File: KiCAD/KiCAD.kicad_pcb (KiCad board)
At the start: 2 copper layers, 200 x 150 mm, 174 parts, among them J1 Conn_01x02_Pin, J10 Paddle, J11 GRID_BIAS, J12 CATHODE_SENSE, J13 Conn_01x05, J14 Conn_01x02_Pin, J15 Conn_01x03_Pin, J2 Conn_01x02_Pin, J3 Conn_01x02_Pin, J4 8P8C_Shielded, J5 ENC_INT if needed, J6 TX/RX, J7 HV, J8 HV_INRUSH_BYPASS, J9 TR_SENSE, Q1 J310, Q2 2N7000, Q3 2N7000, Q4 2N7000, Q5 2N7000, Q6 2N7000, Q7 2N7000, T1 2N3906, T2 2N3906, U1 Si5351A_Breakout, U10 OPA454, U11 LM4040LP-5, U12 LM393, U13 OPA1641, U14 OPA1641, U16 AM26LS32ACN, U17 Adafruit_PCF8575_Breakout, U18 CD14538B, U3 MC1496, U4 MCP4921, U5 OPA454, U6 LM7171xIN, U7 LM7171xIN, U8 MCP4728, U9 LM7805_TO220

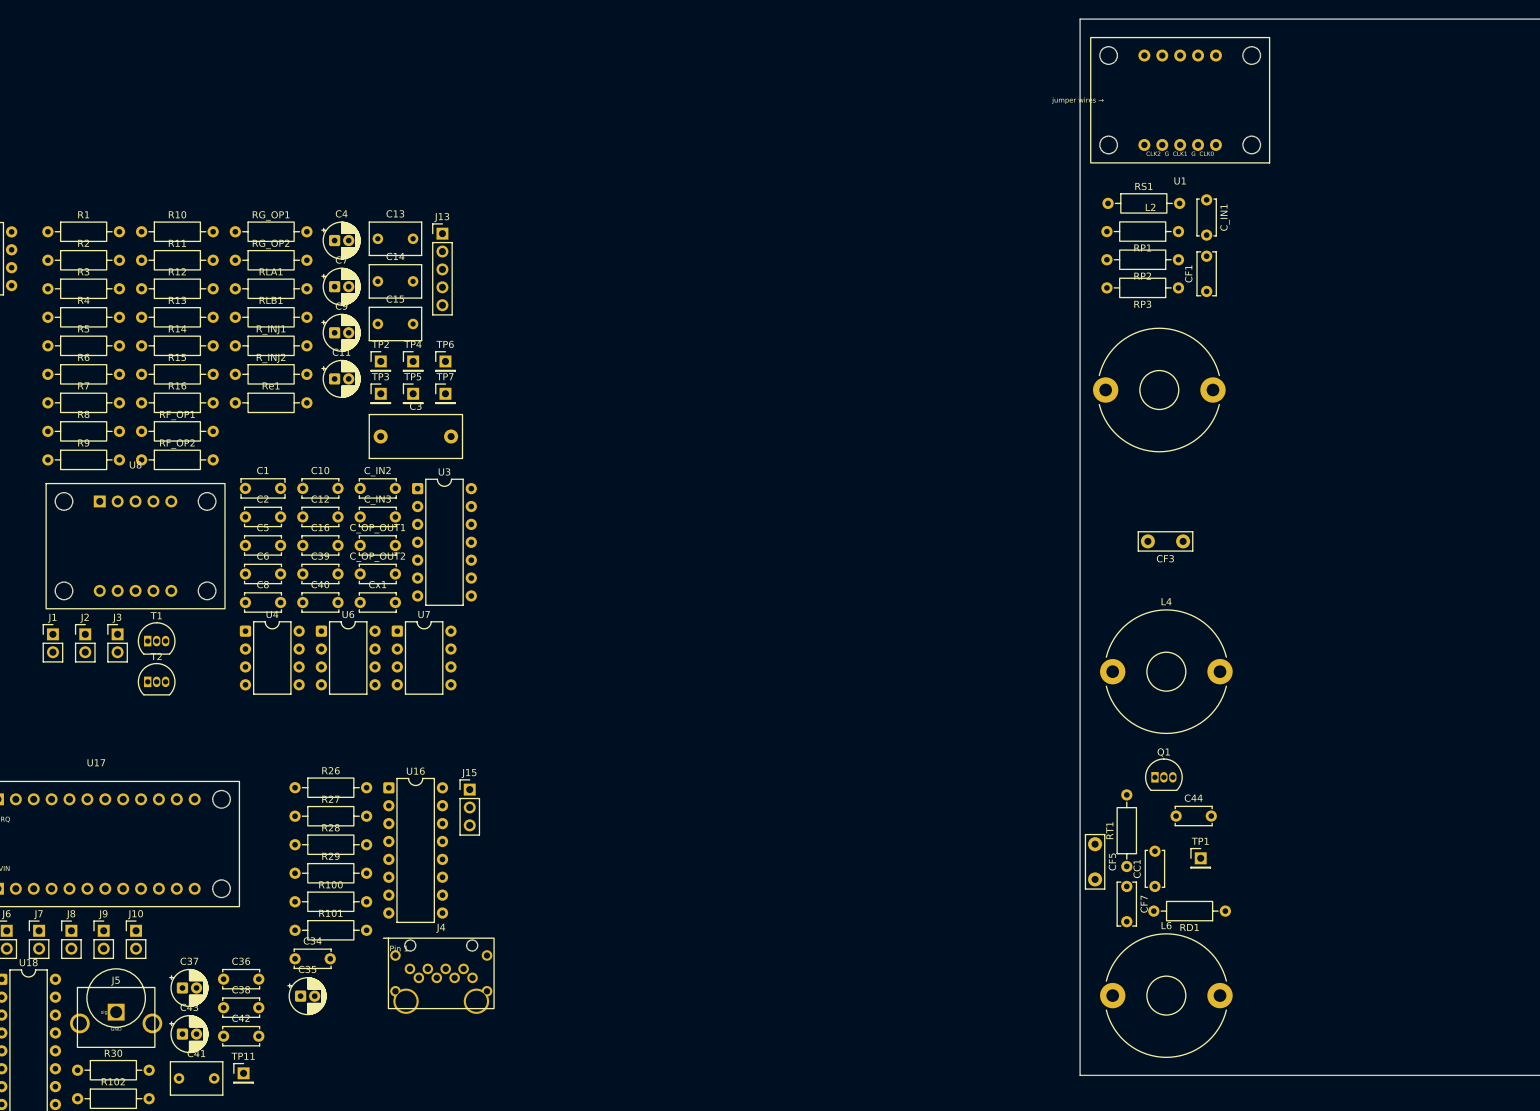
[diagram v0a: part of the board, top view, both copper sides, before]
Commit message: kicad: buffer_keyer partial placement + MCP4728 footprint rebuild
- KiCAD.kicad_pcb: initial placement of 19 buffer_keyer parts (MC1496
  keyer, T1/T2 2N3906s, VEE divider R7/R8, LM4040, C4 10uF bulk, R_INJ1
  and adjacent passives) on the 200x150 board alongside the completed
  VFO block. Zero routing yet.
- Adafruit_MCP4728_Breakout.kicad_mod: rebuild for the correct 2 x 6-pin
  physical layout (was 5+5). Top row JP2 = GND VA VB VC VD VCC, bottom
  row JP1 = VCC GND SCL SDA LDAC RDY. Duplicate VCC/GND pads share
  pad numbers (1,2) so they tie to the same nets as the symbol's VIN/GND.
  Silk labels rebuilt as 12 per-pin fp_text items centered on each pin's
  X coordinate for clear placement verification.
- buffer_keyer.kicad_sch: two 100nF VEE-to-GND decoupling caps added at
  T1 and T2.

Co-Authored-By: Claude Opus 4.7 <noreply@anthropic.com>
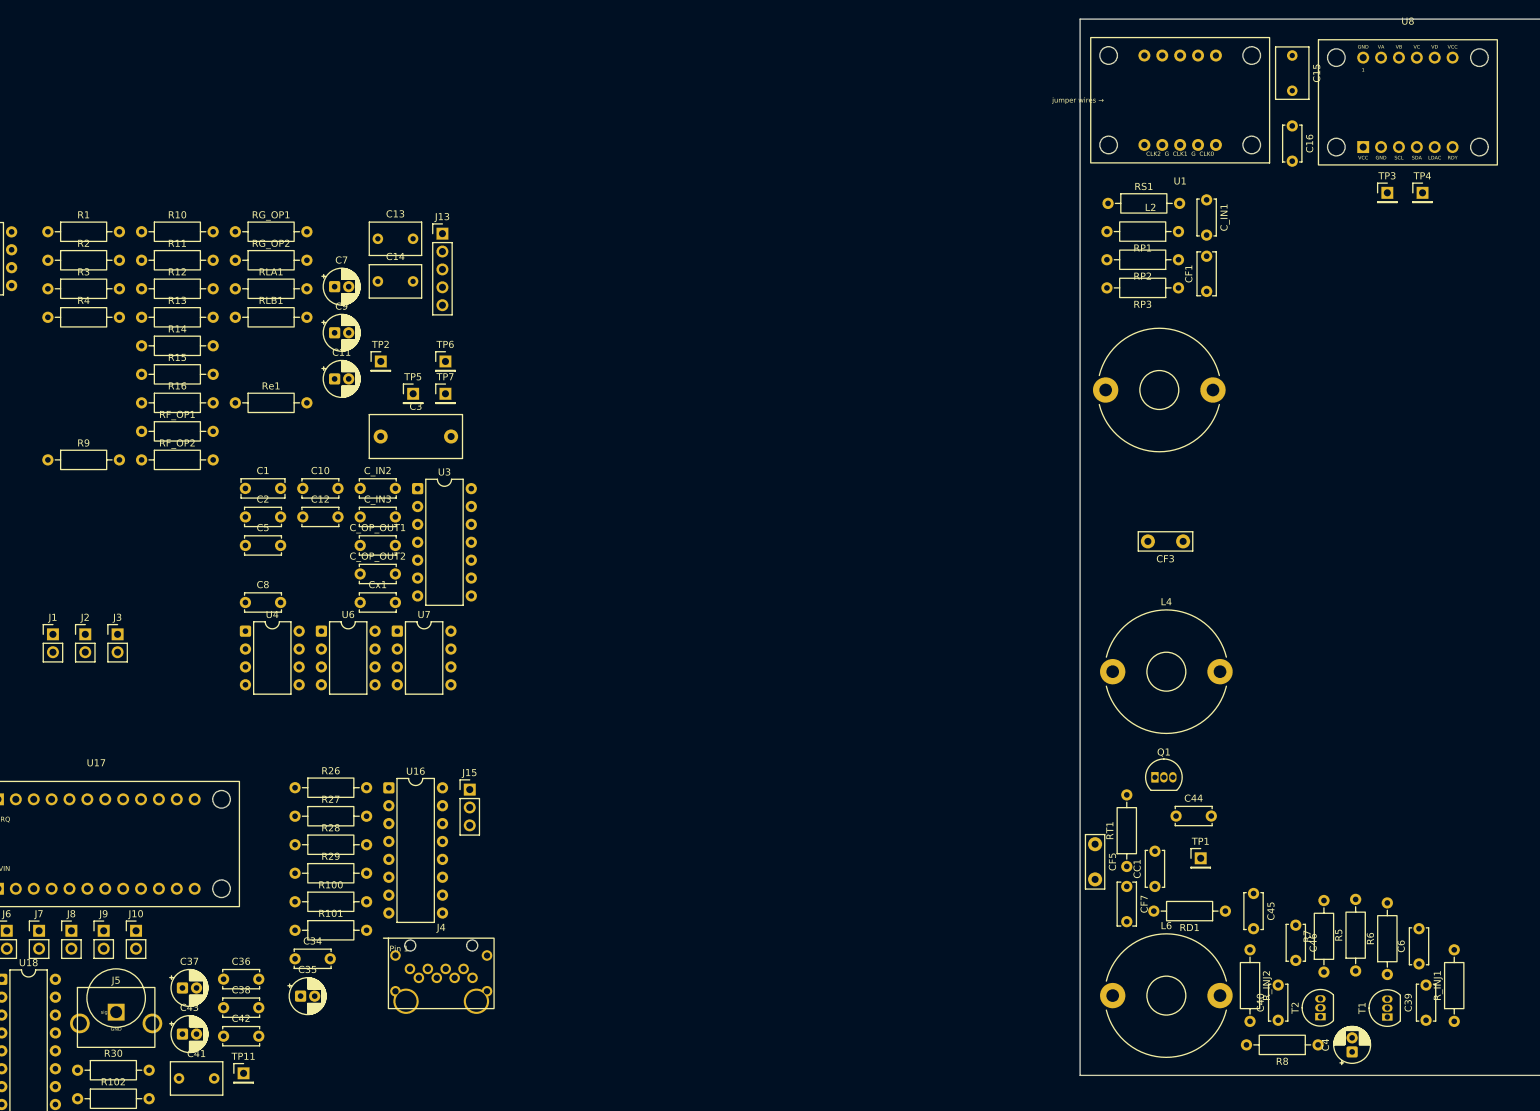
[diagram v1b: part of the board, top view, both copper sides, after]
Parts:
- added C45: 100nF, Capacitor_THT:C_Disc_D5.0mm_W2.5mm_P5.00mm, F.Cu at (40.5, 138.5)
- added C46: 100nF, Capacitor_THT:C_Disc_D5.0mm_W2.5mm_P5.00mm, F.Cu at (46.5, 143.0)
- moved R6 208.4 mm to (59.5, 150.0), turned to 90 degrees
- moved R5 205.8 mm to (55.0, 149.5), turned to 90 degrees
- moved R8 200.3 mm to (49.7, 160.0), turned to 180 degrees
- moved R7 198.4 mm to (50.5, 149.7), turned to 90 degrees
- moved R_INJ1 197.9 mm to (69.0, 156.7), turned to 90 degrees
- moved U8 191.4 mm to (62.4, 26.1)
- moved C4 184.8 mm to (54.5, 161.0), turned to 90 degrees
- moved T1 184.0 mm to (59.5, 156.0), turned to 90 degrees
- moved C6 175.6 mm to (64.0, 148.5), turned to 90 degrees
- moved T2 173.2 mm to (50.0, 156.0), turned to 90 degrees
- moved C39 171.6 mm to (65.0, 156.5), turned to 90 degrees
- moved R_INJ2 165.7 mm to (40.0, 146.5), turned to -90 degrees
- moved C16 152.6 mm to (46.0, 29.5), turned to -90 degrees
- moved C40 150.7 mm to (44.0, 156.5), turned to 90 degrees
- moved TP3 145.8 mm to (59.5, 39.0)
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
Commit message: kicad: T68-6 hand-wound toroid footprints (flat + vertical)
- xmitter.pretty/T68-6_Flat_HandWound.kicad_mod: flat mount for L2/L6.
  Both leads exit on the same radial side -- outer pad at (0, -10.0)
  1.23 mm outside OD, inner pad at (0, -2.5) inside the ID hole.
  Pitch 7.5 mm. Silk shows OD (17.53 mm) + ID (9.40 mm) circles.
- xmitter.pretty/T68-6_Vertical_HandWound.kicad_mod: on-edge mount for L4.
  Top-down projection = OD x HT (17.53 x 4.83 mm) rectangle. Pads at
  (-2.0, -4.5) and (+2.0, +4.5) -- above and below the rectangle with
  the diagonal offset that matches natural lead exit after 4-turn winding.
- vfo.kicad_sch: L2/L4/L6 footprint fields switched to the new project
  footprints (was Inductor_THT:L_Toroid_Horizontal_D17.3mm_P15.24mm_Bourns_2000
  which is a pre-wound Bourns part, not a hand-wound toroid).
- Documentation/flat-toroid.jpg: reference drawing showing lead
  arrangement for both mount styles.

Nominal L per inductor with 4 turns of 22/24 AWG magnet wire evenly
spaced: A_L(T68-6) * 4^2 = 47 * 16 = 752 nH (target 736 nH, +2.2%).

Co-Authored-By: Claude Opus 4.7 <noreply@anthropic.com>
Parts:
- L2, L6: footprint Inductor_THT:L_Toroid_Horizontal_D17.3mm_P15.24mm_Bourns_2000 -> xmitter:T68-6_Flat_HandWound
- L4: footprint Inductor_THT:L_Toroid_Horizontal_D17.3mm_P15.24mm_Bourns_2000 -> xmitter:T68-6_Vertical_HandWound
- moved C1 265.1 mm to (162.4, 75.8)
- moved C10 265.1 mm to (170.6, 75.8)
- moved C11 265.1 mm to (175.1, 60.2)
- moved C12 265.1 mm to (170.6, 79.8)
- moved C13 265.1 mm to (181.2, 40.3)
- moved C14 265.1 mm to (181.2, 46.4)
- moved C2 265.1 mm to (162.4, 79.8)
- moved C5 265.1 mm to (162.4, 83.8)
- moved C7 265.1 mm to (175.1, 47.1)
- moved C8 265.1 mm to (162.4, 92.0)
- moved C9 265.1 mm to (175.1, 53.6)
- moved J13 265.1 mm to (190.4, 39.6)
- moved R1 265.1 mm to (134.4, 39.3)
- moved R10 265.1 mm to (147.7, 39.3)
- moved R11 265.1 mm to (147.7, 43.4)
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
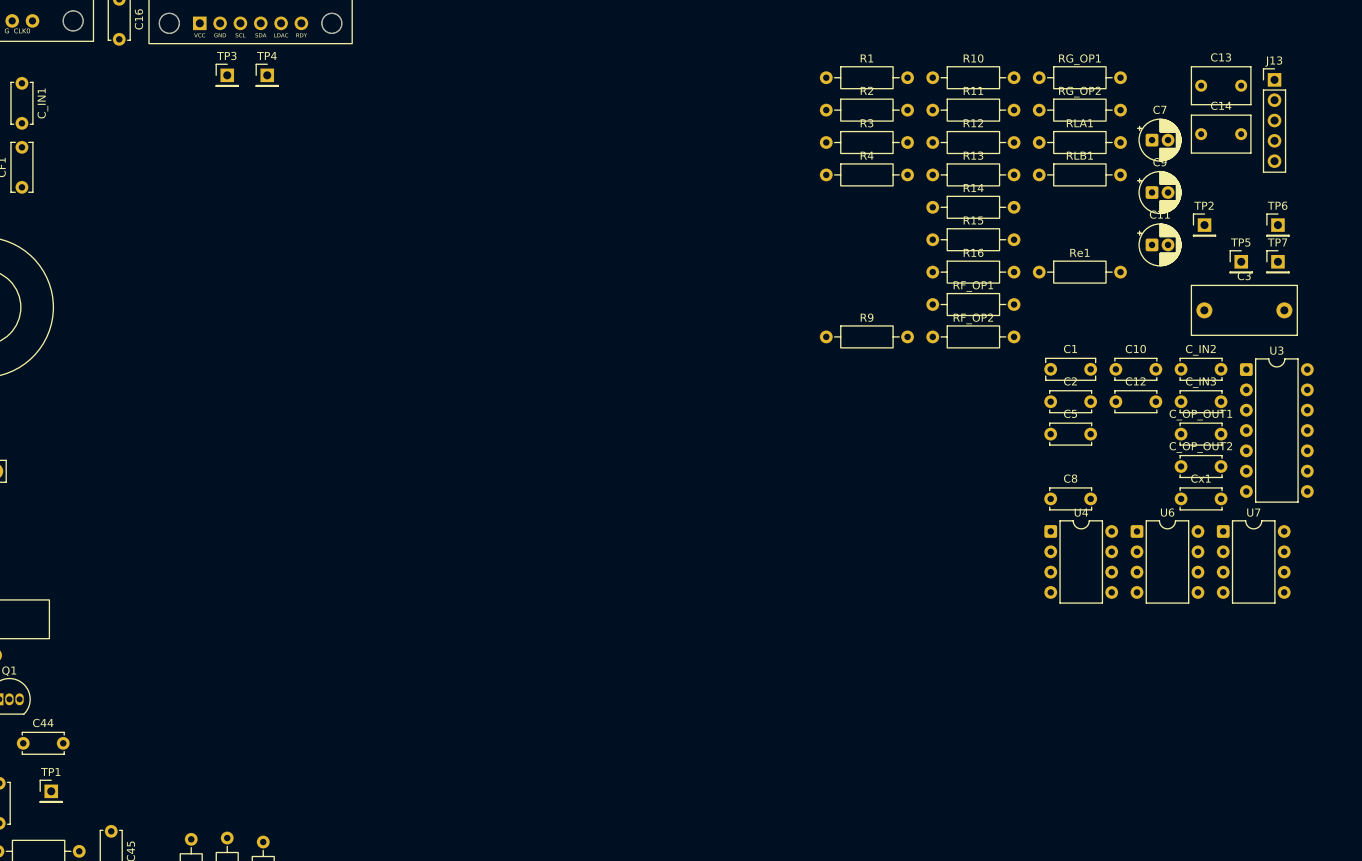
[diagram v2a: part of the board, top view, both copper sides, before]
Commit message: docs: two-box construction plan; kicad: ongoing layout + T1/T2 decoupling
- construction.md: new "Electronics-in-a-separate-box strategy" section.
  Control PCB (MC1496 keyer, MCP4921 DAC, Si5351 VFO, MCP4728 DAC,
  Metro ESP32-S3) goes in a small metal box on top of the main chassis;
  MOD_RF_OUT+/- crosses the gap through bulkhead BNCs on both boxes.
  Recommended part Amphenol RF 112404. Documents the signal chain,
  balance/matching requirements for CW carrier suppression, and the
  grounding scheme (both boxes bonded through the coax shield).
- buffer_keyer.kicad_sch: continued edits including the two 100nF
  VEE-to-GND decoupling caps at T1/T2 noted earlier.
- KiCAD.kicad_pcb: ongoing buffer_keyer placement progress.

Co-Authored-By: Claude Opus 4.7 <noreply@anthropic.com>
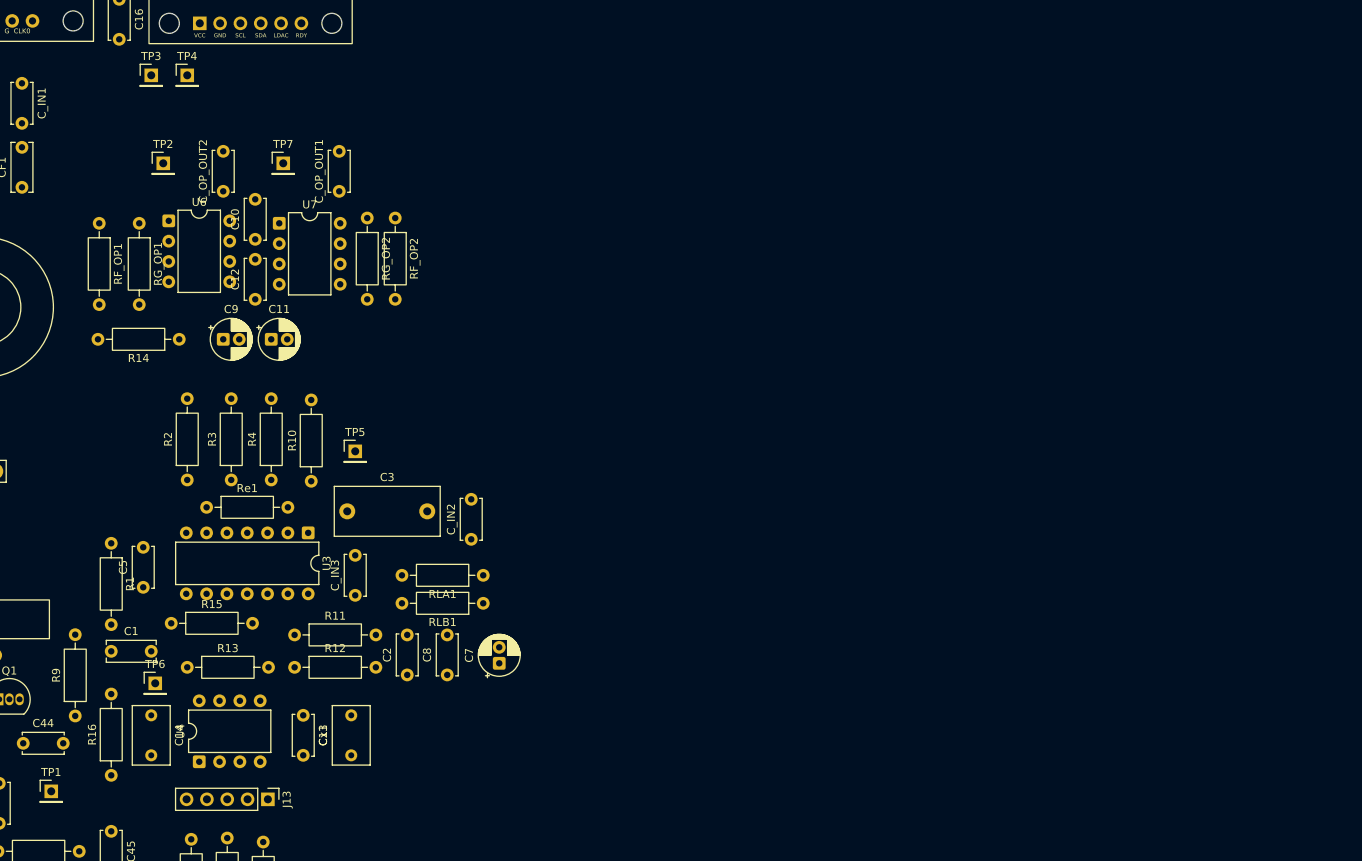
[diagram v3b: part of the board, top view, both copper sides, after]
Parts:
- moved J13 154.7 mm to (64.6, 129.5), turned to -90 degrees
- moved TP6 151.6 mm to (50.5, 115.0)
- moved C14 150.0 mm to (50.0, 119.0), turned to -90 degrees
- moved C13 135.3 mm to (75.0, 124.0), turned to 90 degrees
- moved TP2 130.4 mm to (51.5, 50.0)
- moved U6 127.1 mm to (52.2, 57.2)
- moved TP7 124.9 mm to (66.5, 50.0)
- moved C_OP_OUT2 124.6 mm to (59.0, 53.5), turned to 90 degrees
- moved U7 124.1 mm to (66.0, 57.5)
- moved C1 122.6 mm to (45.0, 111.0)
- moved R16 120.4 mm to (45.0, 126.5), turned to 90 degrees
- moved U3 119.0 mm to (69.6, 96.2), turned to -90 degrees
- moved C9 117.5 mm to (59.0, 72.0)
- moved C5 115.0 mm to (49.0, 103.0), turned to 90 degrees
- moved RG_OP1 114.0 mm to (48.5, 57.5), turned to -90 degrees
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
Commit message: kicad: buffer_keyer part placement complete; component datasheets
- KiCAD.kicad_pcb: placement for VEE generator (U15, U19, C47-C51, L7),
  local LM7805 + bypass caps, and new test points on buffer_keyer
- arduino/buffer_keyer schematics: minor cleanup from PCB update pass
- Documentation/Components: add 78F series, L79L, ICL7660S-A, Wurth
  Elek-caap datasheets for reference

Co-Authored-By: Claude Opus 4.7 <noreply@anthropic.com>
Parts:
- removed J10: Paddle, Connector_PinHeader_2.54mm:PinHeader_1x02_P2.54mm_Vertical
- removed J2: Conn_01x02_Pin, Connector_PinHeader_2.54mm:PinHeader_1x02_P2.54mm_Vertical
- added C47: 0.1uF, Capacitor_THT:C_Disc_D5.0mm_W2.5mm_P5.00mm, F.Cu at (91.0, 38.5)
- added C48: 10uF, Capacitor_THT:CP_Radial_D5.0mm_P2.00mm, F.Cu at (112.5, 21.0)
- added C49: 100uF, Capacitor_THT:CP_Radial_D6.3mm_P2.50mm, F.Cu at (103.5, 21.5)
- added C50: 10uF, Capacitor_THT:CP_Radial_D5.0mm_P2.00mm, F.Cu at (85.5, 39.0)
- added C51: 100nF, Capacitor_THT:C_Disc_D5.0mm_W2.5mm_P5.00mm, F.Cu at (105.0, 42.5)
- added C52: 0.33uF, Capacitor_THT:C_Rect_L7.0mm_W3.5mm_P5.00mm, F.Cu at (112.0, 38.0)
- added C53: 0.1uF, Capacitor_THT:C_Disc_D5.0mm_W2.5mm_P5.00mm, F.Cu at (83.0, 23.5)
- added J16: Conn_01x05, Connector_PinHeader_2.54mm:PinHeader_1x05_P2.54mm_Vertical, F.Cu at (78.5, 18.0)
- added J3: Conn_01x02_Pin, Connector_PinHeader_2.54mm:PinHeader_1x02_P2.54mm_Vertical, F.Cu at (102.4, 44.9)
- added L7: 22uH, Inductor_THT:L_Axial_L7.0mm_D3.3mm_P10.16mm_Horizontal_Fastron_MICC, F.Cu at (106.0, 27.9)
- added TP12: LDAC, Connector_PinHeader_2.54mm:PinHeader_1x01_P2.54mm_Vertical, F.Cu at (65.0, 41.0)
- added TP13: T2 out, Connector_PinHeader_2.54mm:PinHeader_1x01_P2.54mm_Vertical, F.Cu at (66.5, 156.0)
- added TP14: T1 out, Connector_PinHeader_2.54mm:PinHeader_1x01_P2.54mm_Vertical, F.Cu at (71.0, 156.0)
- added TP15: Key_Out, Connector_PinHeader_2.54mm:PinHeader_1x01_P2.54mm_Vertical, F.Cu at (40.5, 86.5)
- added TP16: TX/RX, Connector_PinHeader_2.54mm:PinHeader_1x01_P2.54mm_Vertical, F.Cu at (120.5, 68.0)
- added TP17: HV, Connector_PinHeader_2.54mm:PinHeader_1x01_P2.54mm_Vertical, F.Cu at (120.5, 73.0)
- added TP18: Inrush, Connector_PinHeader_2.54mm:PinHeader_1x01_P2.54mm_Vertical, F.Cu at (120.5, 78.0)
- added TP19: HB trigger, Connector_PinHeader_2.54mm:PinHeader_1x01_P2.54mm_Vertical, F.Cu at (120.5, 84.0)
- added TP20: VEE, Connector_PinHeader_2.54mm:PinHeader_1x01_P2.54mm_Vertical, F.Cu at (88.0, 49.5)
- added TP21: +5V, Connector_PinHeader_2.54mm:PinHeader_1x01_P2.54mm_Vertical, F.Cu at (87.0, 61.0)
- added TP22: OUT-, Connector_PinHeader_2.54mm:PinHeader_1x01_P2.54mm_Vertical, F.Cu at (76.0, 73.0)
- added TP23: OUT+, Connector_PinHeader_2.54mm:PinHeader_1x01_P2.54mm_Vertical, F.Cu at (83.5, 85.5)
- added U15: LM7805_TO220, Package_TO_SOT_THT:TO-220-3_Vertical, F.Cu at (80.5, 31.5)
- added U19: L79L08_TO92, Package_TO_SOT_THT:TO-92_Inline, F.Cu at (96.5, 43.5)
- added U20: ICL7660S, Package_DIP:DIP-8_W7.62mm, F.Cu at (93.0, 34.0)
- moved J5 272.1 mm to (120.5, 30.0), turned to -90 degrees
- moved R102 267.7 mm to (113.5, 49.0)
- moved J6 260.0 mm to (120.5, 104.5)
- moved J7 254.4 mm to (120.5, 112.5)
- moved Q4 252.9 mm to (105.7, 100.9)
- moved Q6 252.7 mm to (106.2, 116.9)
- moved Q5 252.7 mm to (105.7, 108.4)
- moved Q7 252.2 mm to (106.2, 125.9)
- moved C38 251.2 mm to (118.0, 40.5)
- moved J8 249.0 mm to (120.5, 120.5)
- moved J9 242.8 mm to (87.5, 22.5), turned to 90 degrees
- moved J1 238.7 mm to (93.5, 18.0), turned to 90 degrees
- moved U17 238.6 mm to (107.8, 74.4), turned to -90 degrees
- moved U18 223.5 mm to (84.0, 119.2)
- moved C37 219.9 mm to (93.0, 71.5), turned to 90 degrees
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
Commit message: kicad: additional placement tweaks on analog board
Follow-on placement adjustments after the buffer_keyer VEE-generator
part additions.

Co-Authored-By: Claude Opus 4.7 <noreply@anthropic.com>
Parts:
- moved C37 4.91 mm to (88.5, 69.5), turned to 0 degrees
- moved TP5 1.12 mm to (76.0, 85.0)
